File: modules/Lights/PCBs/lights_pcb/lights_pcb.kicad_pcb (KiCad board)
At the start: 2 copper layers, 89 x 100 mm, 57 parts, among them J1 THONKICONN, J10 Conn_02x04_Top_Bottom, J11 Conn_02x04_Top_Bottom, J12 Conn_02x02_Top_Bottom, J13 Conn_02x02_Top_Bottom, J2 THONKICONN, J3 THONKICONN, J4 THONKICONN, J5 Conn_01x04_Pin, J6 Conn_01x03_Pin, J8 Barrel_Jack, J9 Eurorack_2x8_Power, Q1 RFP30N06LE, Q2 RFP30N06LE, Q3 RFP30N06LE, Q7 2N7000, Q8 2N7000, SW1 TL1105SPF250Q, SW2 SW_SPDT, U1 MCP6004, U2 SN74LVC1G3157DCKR, U3 ISO6740, U4 LM4040BIZ-5, U5 LM4040BIZ-5

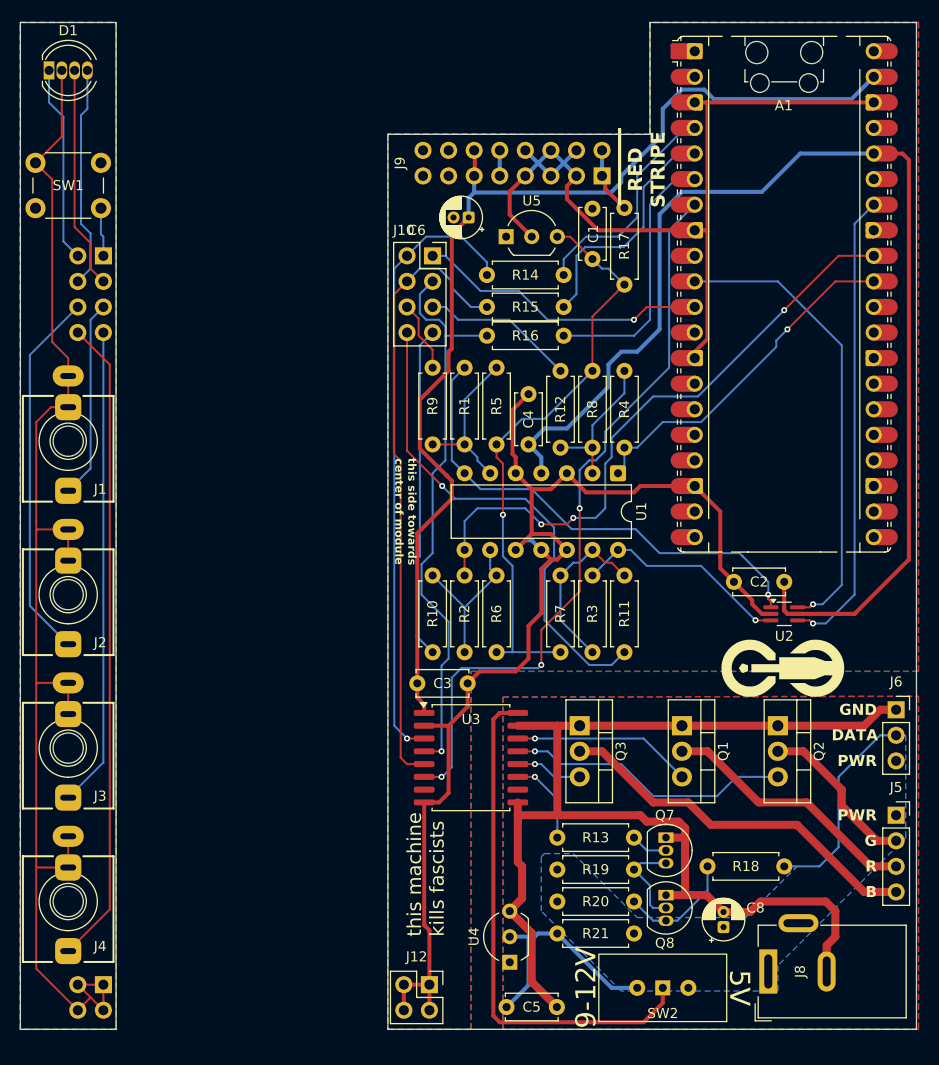
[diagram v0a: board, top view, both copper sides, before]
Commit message: Switch lights to external 3.3V power supply instead of using rpi pico
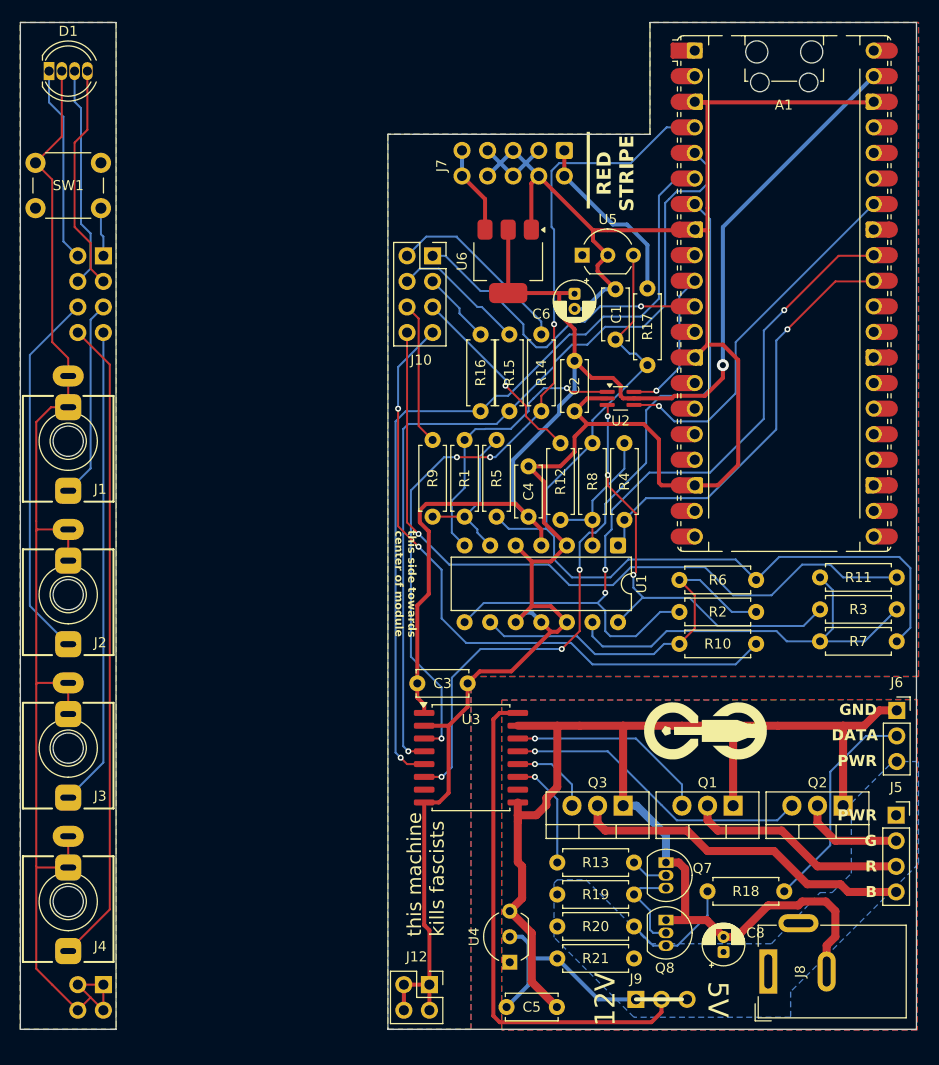
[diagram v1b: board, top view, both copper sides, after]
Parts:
- removed SW2: SW_SPDT, Button_Switch_THT:SW_Slide-03_Wuerth-WS-SLTV_10x2.5x6.4_P2.54mm
- added J7: Eurorack_2x5_Power, Connector_IDC:IDC-Header_2x05_P2.54mm_Vertical, F.Cu at (112.8, 44.5)
- added U6: LM1117MP-3.3, Package_TO_SOT_SMD:SOT-223-3_TabPin2, F.Cu at (107.2, 55.5)
- D1: value LED_RKBG -> LED_RKGB
- J9: value Eurorack_2x8_Power -> Conn_01x03_Pin; footprint Connector_PinSocket_2.54mm:PinSocket_2x08_P2.54mm_Horizontal -> Connector_PinSocket_2.54mm:PinSocket_1x03_P2.54mm_Vertical
- moved J9 81.9 mm to (119.9, 128.8), turned to 90 degrees
- moved R7 33.4 mm to (145.8, 93.2), turned to 180 degrees
- moved R10 32.1 mm to (131.8, 93.5), turned to 180 degrees
- moved R3 30.5 mm to (145.8, 90.0), turned to 180 degrees
- moved C2 30.3 mm to (113.8, 65.4), turned to -90 degrees
- moved R2 29.2 mm to (131.8, 90.3), turned to 180 degrees
- moved R11 28.1 mm to (145.8, 86.9), turned to 180 degrees
- moved U2 26.9 mm to (118.4, 69.1)
- moved R6 26.8 mm to (131.8, 87.1), turned to 180 degrees
- moved C6 13.0 mm to (113.8, 58.7), turned to -90 degrees
- moved Q2 10.2 mm to (140.5, 109.5), turned to 180 degrees
- moved G1 9.89 mm to (127.3, 102.1)
- moved Q1 9.43 mm to (129.5, 109.5), turned to 180 degrees
- moved Q3 9.04 mm to (118.6, 109.5), turned to 180 degrees
- moved C1 8.32 mm to (117.9, 63.2)
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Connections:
- A1 pad 36: /Rear Board/+3.3V -> unconnected-(A1-3V3-Pad36)
- A1 pad 39: /Rear Board/+5V -> /Rear Board/+3.3V
- A1 pad 4: Net-(A1-GPIO2) -> /Rear Board/PWM_SIGNAL_R
- A1 pad 5: Net-(A1-GPIO3) -> /Rear Board/PWM_SIGNAL_G
- A1 pad 6: Net-(A1-GPIO4) -> /Rear Board/PWM_SIGNAL_B
- C3 pad 1: /Rear Board/+5V -> /Rear Board/+3.3V
- C5 pad 1: Net-(SW2-A) -> Net-(J9-Pin_1)
- C6 pad 1: /Rear Board/+5V -> /Rear Board/+3.3V
- D1 pad 3: /Front Board/LED_B -> /Front Board/LED_G
- D1 pad 4: /Front Board/LED_G -> /Front Board/LED_B
- J9 pad 1: /Rear Board/-12V -> Net-(J9-Pin_1)
- J9 pad 2: /Rear Board/-12V -> /Rear Board/LED Driver/LED_5V
- J9 pad 3: /Rear Board/GND -> /Rear Board/LED Driver/LED_PWR
- R14 pad 2: Net-(A1-GPIO2) -> /Rear Board/PWM_SIGNAL_R
- R15 pad 2: Net-(A1-GPIO3) -> /Rear Board/PWM_SIGNAL_G
- R16 pad 2: Net-(A1-GPIO4) -> /Rear Board/PWM_SIGNAL_B
- R21 pad 2: Net-(SW2-A) -> Net-(J9-Pin_1)
- U3 pad 1: /Rear Board/+5V -> /Rear Board/+3.3V
- U3 pad 3: /Rear Board/LED_R -> /Rear Board/PWM_SIGNAL_R
- U3 pad 4: /Rear Board/LED_B -> /Rear Board/PWM_SIGNAL_G
- U3 pad 5: /Rear Board/LED_G -> /Rear Board/PWM_SIGNAL_B
- U4 pad 2: Net-(SW2-A) -> Net-(J9-Pin_1)
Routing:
- net /Rear Board/+5V: track 108.4 -> 0.00 mm
- net /Rear Board/PWM_SIGNAL_R: track 0.00 -> 84.4 mm, vias 0 -> 4
- net /Rear Board/PWM_SIGNAL_G: track 0.00 -> 83.9 mm, vias 0 -> 1
- net /Rear Board/PWM_SIGNAL_B: track 0.00 -> 81.9 mm, vias 0 -> 1
- net /Rear Board/LED_B: track 57.2 -> 7.24 mm, vias 1 -> 0
- net /Rear Board/LED_G: track 61.1 -> 13.4 mm
- net /Rear Board/LED_R: track 61.7 -> 18.9 mm, vias 1 -> 0
- net /Rear Board/CV_G: track 33.1 -> 65.6 mm, vias 0 -> 2
- net Net-(A1-GPIO7): track 47.0 -> 14.8 mm
- net /Rear Board/VREF_-5: track 58.7 -> 89.5 mm, vias 1 -> 0
- net Net-(A1-GPIO4): track 26.2 -> 0.00 mm
- net /Rear Board/GND: track 206.4 -> 231.8 mm
- net Net-(U1D--): track 17.4 -> 41.8 mm
- net /Rear Board/CV_B: track 49.4 -> 73.8 mm
- net Net-(A1-GPIO3): track 23.9 -> 0.00 mm
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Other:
- board text added: "12V"
- board text added: "Free Modular Lights back v0.3"
- board text added: "Free Modular Lights front v0.3"
- board text removed: "9-12V"
- board text removed: "Free Modular Lights back v0.2"
- board text removed: "Free Modular Lights front v0.1"
